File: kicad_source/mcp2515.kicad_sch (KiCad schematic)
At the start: 15 parts, among them CN4 SM04B-GHS-TB, CN5 SM04B-GHS-TB, U8 MCP2515T-I/SO, U9 SN65HVD230, Y1 X322516MLB4SI

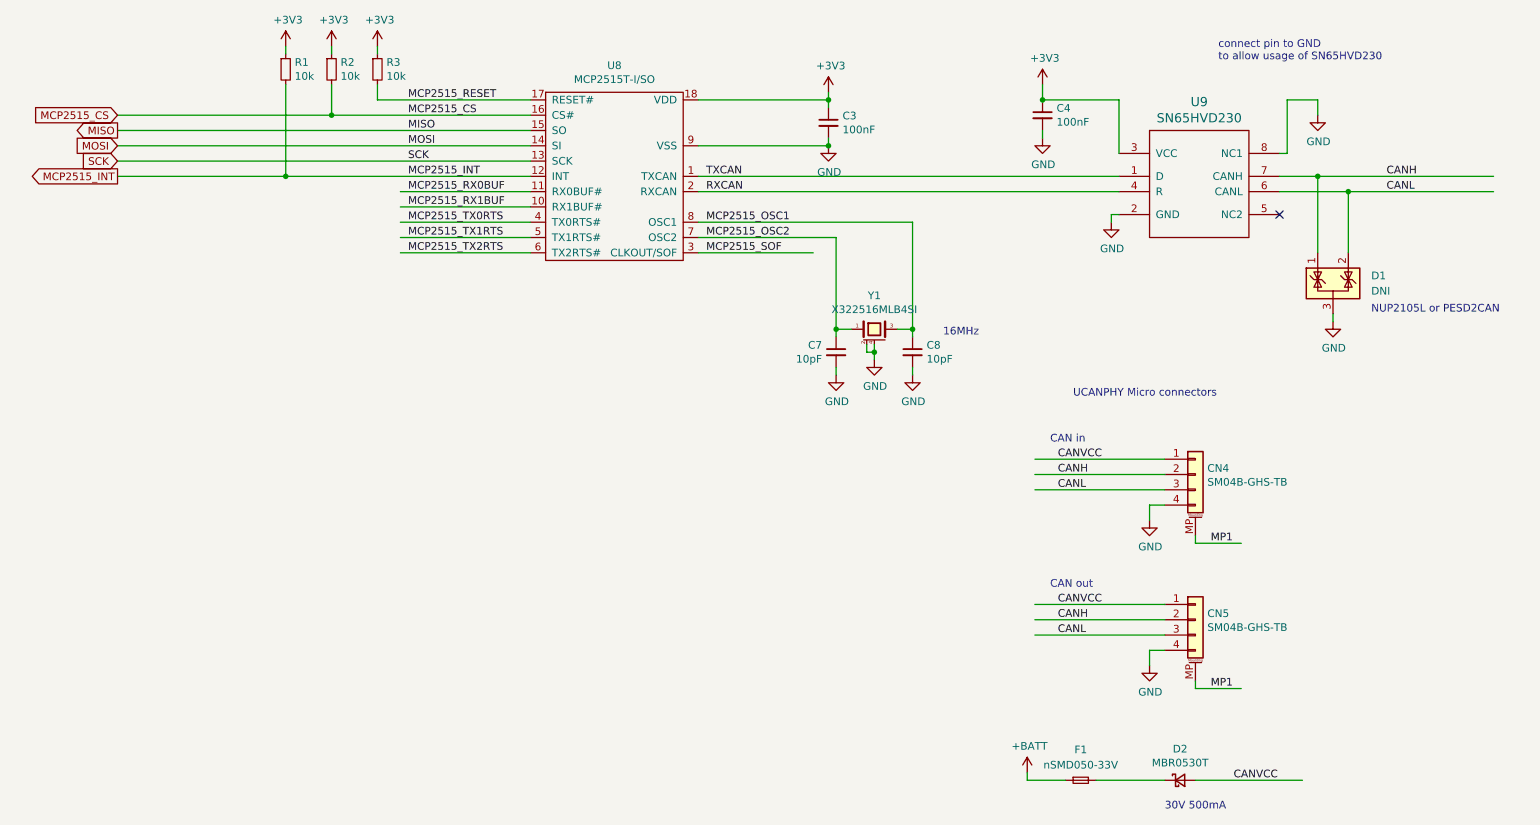
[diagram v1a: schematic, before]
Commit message: added encoder, mounting holes for display at correct position
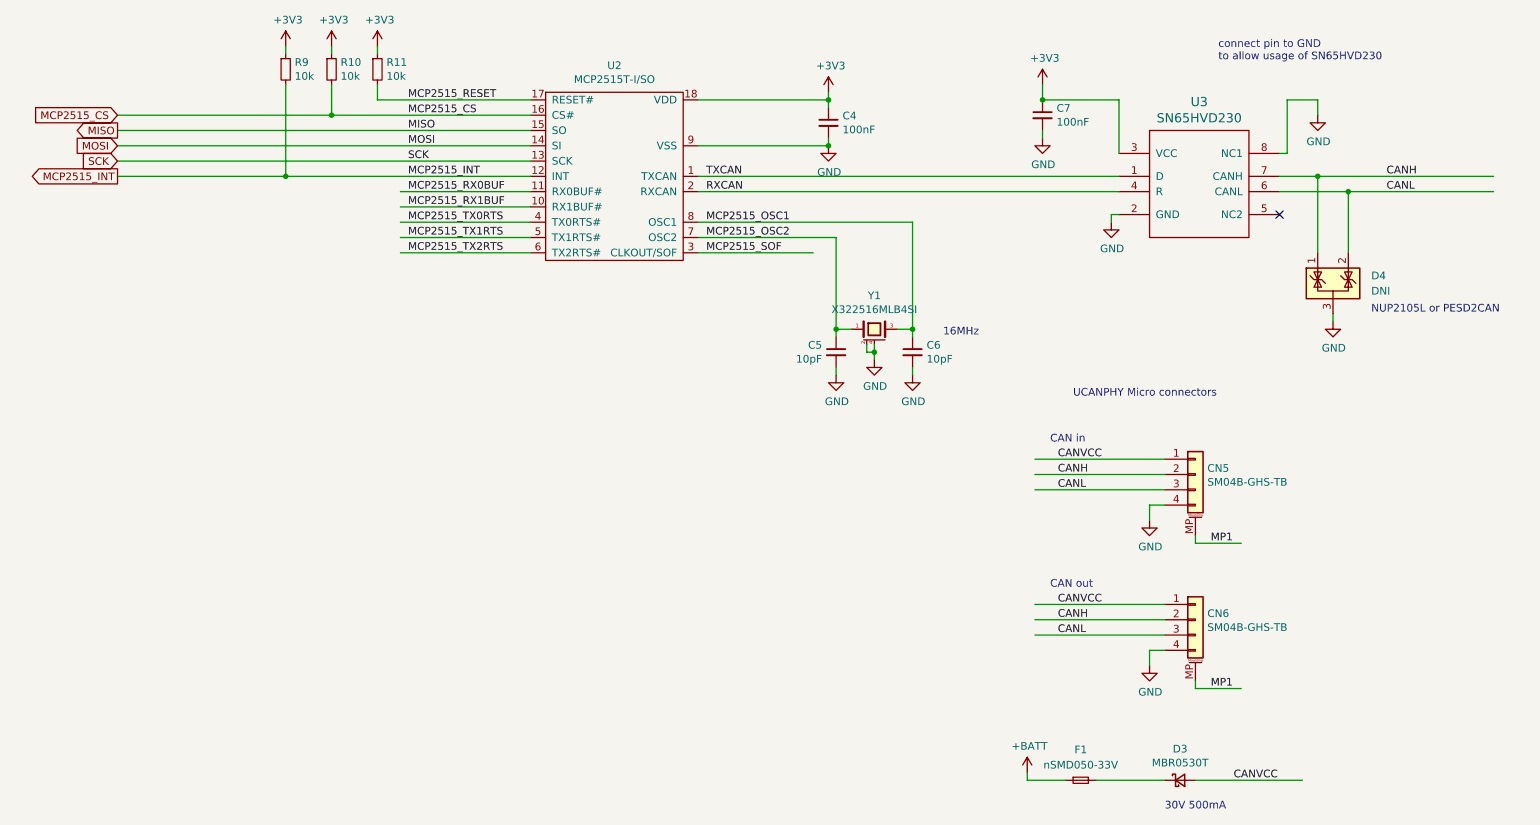
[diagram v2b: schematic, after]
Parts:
- renumbered C3 to C4, C7 to C5, C8 to C6, C4 to C7, CN4 to CN5, CN5 to CN6, D2 to D3, D1 to D4, R2 to R10, R3 to R11, R1 to R9, U8 to U2, U9 to U3

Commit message: added push button
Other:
- title: CyphalIMUBase/CAN -> CyphalHMIBase/CAN
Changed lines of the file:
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@@
 	(paper "A4")
 	(title_block
-		(title "CyphalIMUBase/CAN")
+		(title "CyphalHMIBase/CAN")
 		(date "2026-06-05")
 		(rev "0.1")
